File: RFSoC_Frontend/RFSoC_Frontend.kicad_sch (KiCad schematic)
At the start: 64 parts, among them J1 Conn_Coaxial, J2 Conn_Coaxial, J3 Conn_Coaxial, J4 Conn_Coaxial, J5 Conn_Coaxial, J6 Conn_Coaxial, J7 Conn_Coaxial, J8 Conn_Coaxial, U1 TCM2-33WX+, U2 TCM2-33WX+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

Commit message: updates
updated 3d footprints
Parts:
- C1, C10, C11, C12, C13, C14, C15, C16, C2, C3, C4, C5, C6, C7, C8, C9: Mouser Part Number (none) -> 963-LMF105B7103KVHF
- R1, R13, R14, R15, R16, R17, R18, R19, R2, R20, R29, R3, R30, R31, R32, R4: Mouser Part Number (none) -> 667-ERA-2AEB5900X
- R10, R11, R12, R21, R22, R23, R24, R25, R26, R27, R28, R5, R6, R7, R8, R9: Mouser Part Number (none) -> 71-CRCW0402-17.4-E3
- U1, U2, U3, U4, U5, U6, U7, U8: Mouser Part Number (none) -> 139-TCM2-33WX

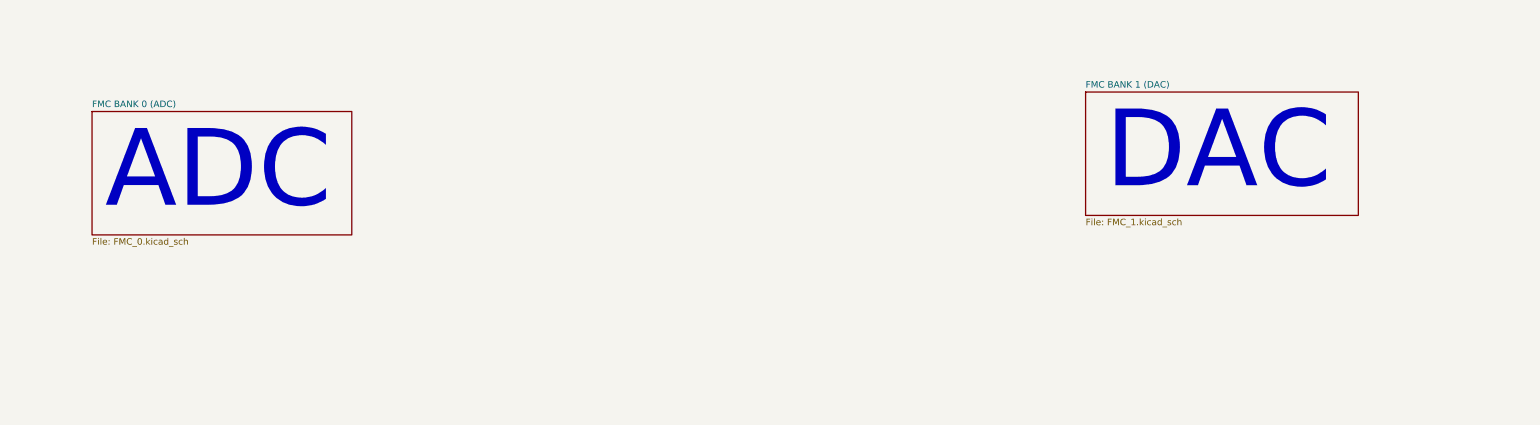
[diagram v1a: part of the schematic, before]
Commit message: fixed grounded util 3v3 pins on the LPAM Cnctr
updated to REV B
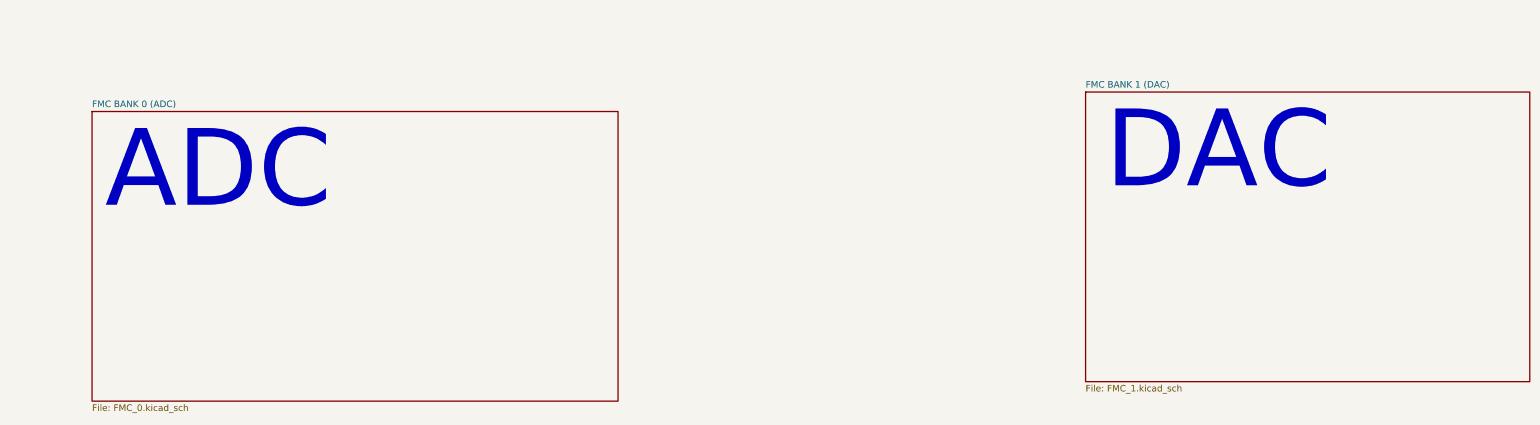
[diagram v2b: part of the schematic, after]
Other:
- company: (none) -> ASU
- title: (none) -> rfsoc front-end
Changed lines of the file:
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@@
 (kicad_sch (version 20211123) (generator eeschema)
   (paper "C")
+  (title_block
+    (title "rfsoc front-end")
+    (date "2022-09-16")
+    (rev "B")
+    (company "ASU")
+    (comment 1 "Updated to fix grounded util-3v3 bus schematic error")
+  )
   (junction (at 86.36 193.04) (diameter 0) (color 0 0 0 0)
   )
@@
     (pin "2")
   )
-  (sheet (at 93.98 234.95) (size 50.8 24.13) (fields_autoplaced)
+  (sheet (at 93.98 234.95) (size 102.87 56.642) (fields_autoplaced)
     (stroke (width 0) (type solid) (color 0 0 0 0))
     (fill (color 0 0 0 0.0000))
@@
       (effects (font (size 1.27 1.27)) (justify left bottom))
     )
-    (property "Sheet file" "FMC_0.kicad_sch" (id 1) (at 93.98 259.6646 0)
+    (property "Sheet file" "FMC_0.kicad_sch" (id 1) (at 93.98 292.1766 0)
       (effects (font (size 1.27 1.27)) (justify left top))
     )
   )
-  (sheet (at 288.29 231.14) (size 53.34 24.13) (fields_autoplaced)
+  (sheet (at 288.29 231.14) (size 86.868 56.642) (fields_autoplaced)
     (stroke (width 0) (type solid) (color 0 0 0 0))
     (fill (color 0 0 0 0.0000))
@@
       (effects (font (size 1.27 1.27)) (justify left bottom))
     )
-    (property "Sheet file" "FMC_1.kicad_sch" (id 1) (at 288.29 255.8546 0)
+    (property "Sheet file" "FMC_1.kicad_sch" (id 1) (at 288.29 288.3666 0)
       (effects (font (size 1.27 1.27)) (justify left top))
     )
@@
       (reference "#PWR0224") (unit 1) (value "GND") (footprint "")
     )
-    (path "/00000000-0000-0000-0000-0000604828d0/3350fca3-65f8-4d10-9fa9-abe5b6f9cf93"
-      (reference "#PWR0225") (unit 1) (value "GND") (footprint "")
-    )
     (path "/00000000-0000-0000-0000-0000604828d0/e287642c-deed-4fba-bf77-c71f0df7028d"
       (reference "#PWR0226") (unit 1) (value "GND") (footprint "")
@@
       (reference "#PWR0239") (unit 1) (value "GND") (footprint "")
     )
-    (path "/00000000-0000-0000-0000-00006049b2da/1f5cfb06-af34-46d4-b50e-b49be107462c"
-      (reference "#PWR0240") (unit 1) (value "GND") (footprint "")
-    )
     (path "/00000000-0000-0000-0000-00006049b2da/ef1ed020-cc9c-4589-8918-fa63043e857d"
       (reference "#PWR0241") (unit 1) (value "GND") (footprint "")
@@
       (reference "#PWR0321") (unit 1) (value "GND") (footprint "")
     )
-    (path "/00000000-0000-0000-0000-00006049b2da/bde62ce2-d82b-4cd1-91f0-a3ec44008bb2"
-      (reference "#PWR0322") (unit 1) (value "GND") (footprint "")
-    )
     (path "/00000000-0000-0000-0000-00006049b2da/1c5586e9-766a-4d69-9175-4ec76a8e4c63"
